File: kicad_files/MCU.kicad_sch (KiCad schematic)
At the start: 25 parts, among them SW1 SW_Push, SW2 SW_Push, U1 STM32F407VGTx, Y1 LFXTAL036869Reel 8MHz Crystal

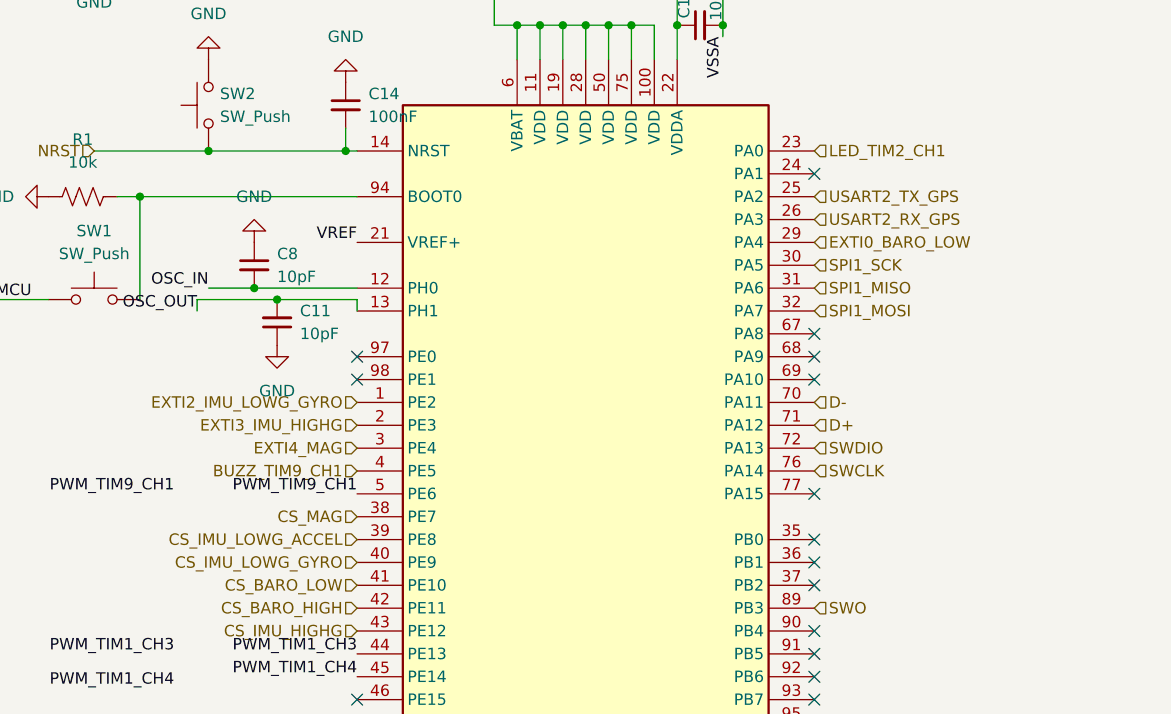
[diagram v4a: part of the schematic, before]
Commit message: switch sensor interrupts
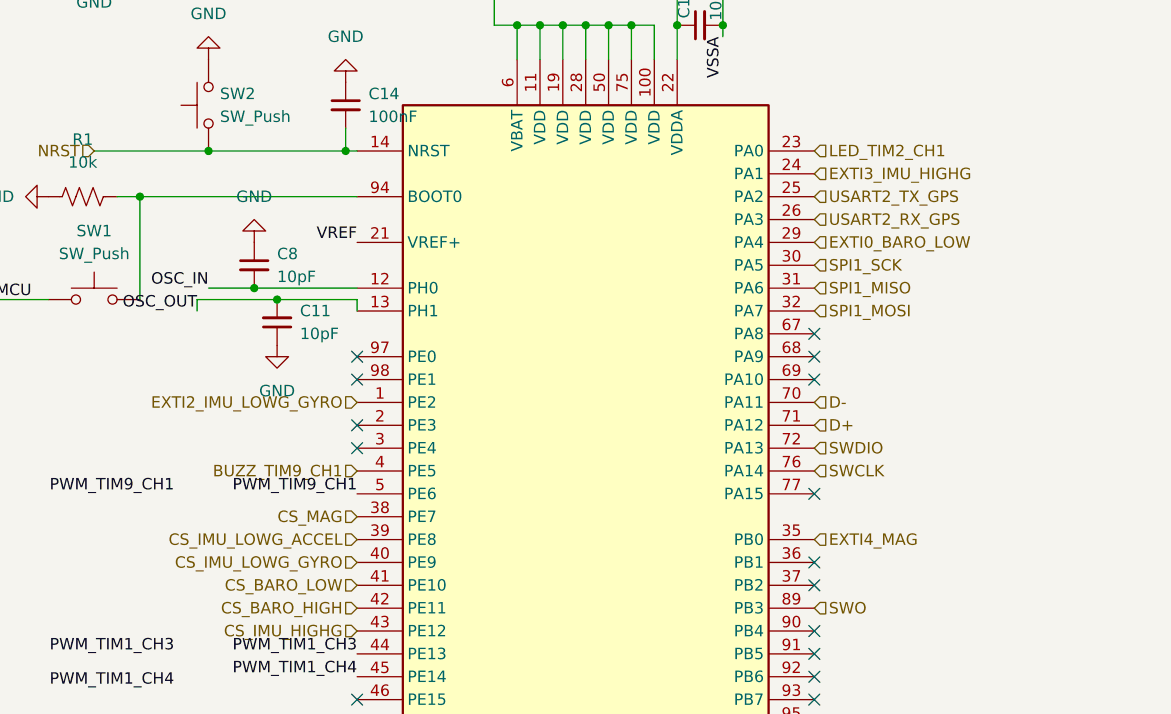
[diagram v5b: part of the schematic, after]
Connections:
- net EXTI3_IMU_HIGHG: now also U1.24 (PA1); no longer U1.2 (PE3)
- net EXTI4_MAG: now also U1.35 (PB0); no longer U1.3 (PE4)
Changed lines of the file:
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@@
-	)
-	(no_connect
-		(at 250.19 137.16)
 	)
 	(no_connect
@@
 	)
 	(no_connect
-		(at 250.19 96.52)
-	)
-	(no_connect
 		(at 250.19 119.38)
 	)
@@
 	)
 	(no_connect
+		(at 199.39 127)
+	)
+	(no_connect
 		(at 199.39 170.18)
 	)
@@
 	(no_connect
 		(at 199.39 185.42)
+	)
+	(no_connect
+		(at 199.39 124.46)
 	)
 	(no_connect
@@
 	(hierarchical_label "EXTI4_MAG"
 		(shape input)
-		(at 199.39 127 180)
-		(effects
-			(font
-				(size 1.27 1.27)
-			)
-			(justify right)
+		(at 250.19 137.16 0)
+		(effects
+			(font
+				(size 1.27 1.27)
+			)
+			(justify left)
 		)
 	)
@@
 	(hierarchical_label "EXTI3_IMU_HIGHG"
 		(shape input)
-		(at 199.39 124.46 180)
-		(effects
-			(font
-				(size 1.27 1.27)
-			)
-			(justify right)
-		)
-	)
+		(at 250.19 96.52 0)
+		(effects
+			(font
+				(size 1.27 1.27)
+			)
+			(justify left)
+		)
+	)

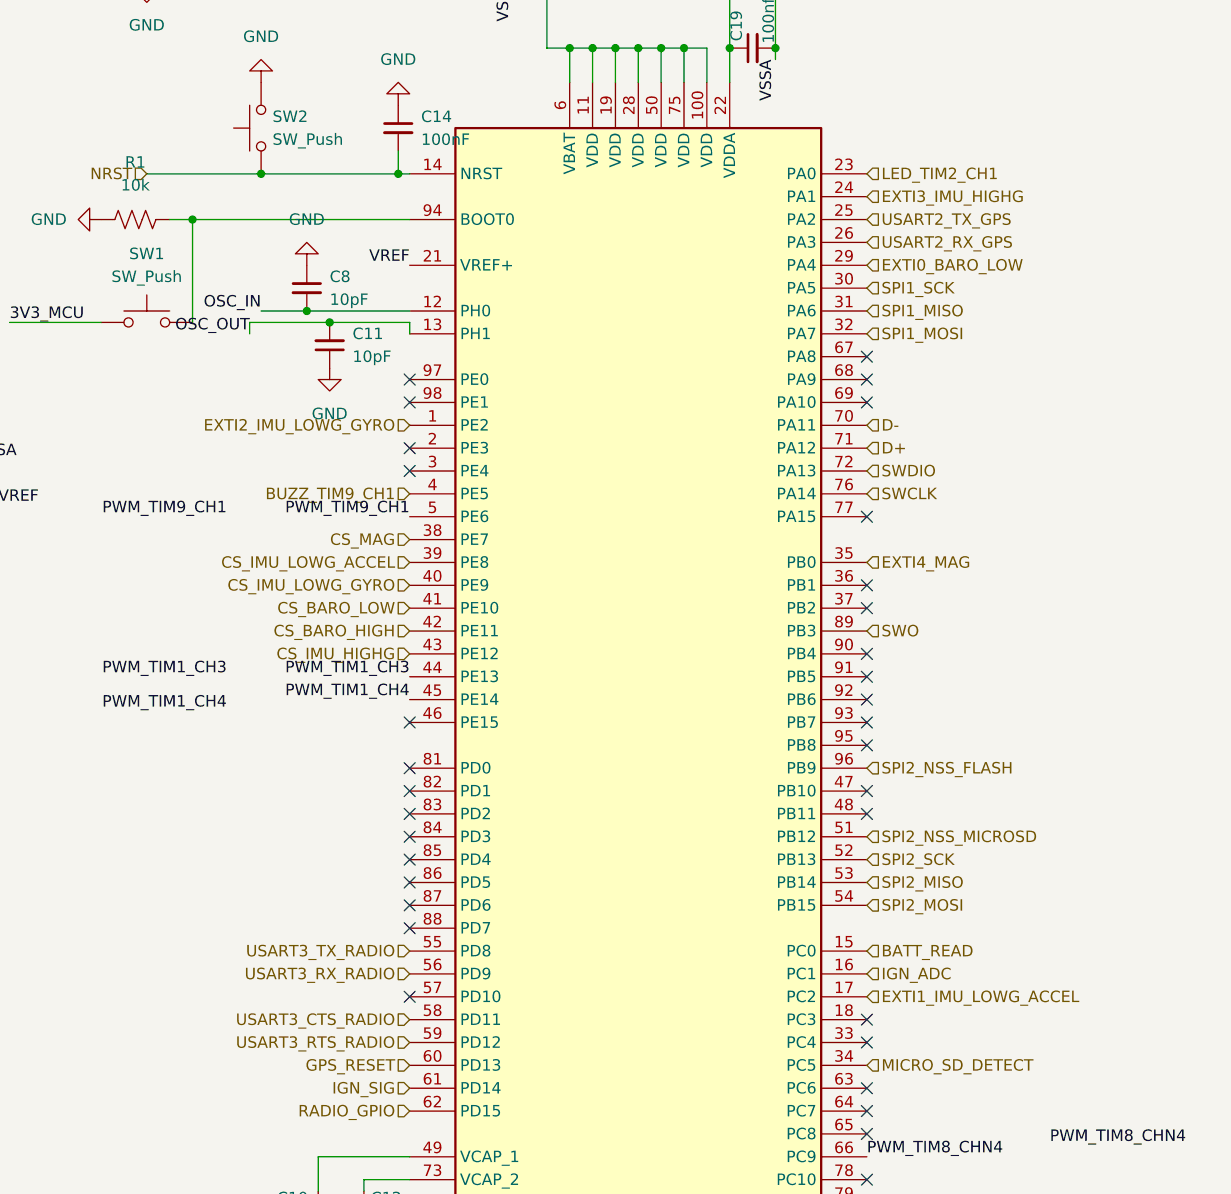
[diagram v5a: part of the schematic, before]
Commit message: changed led, tim
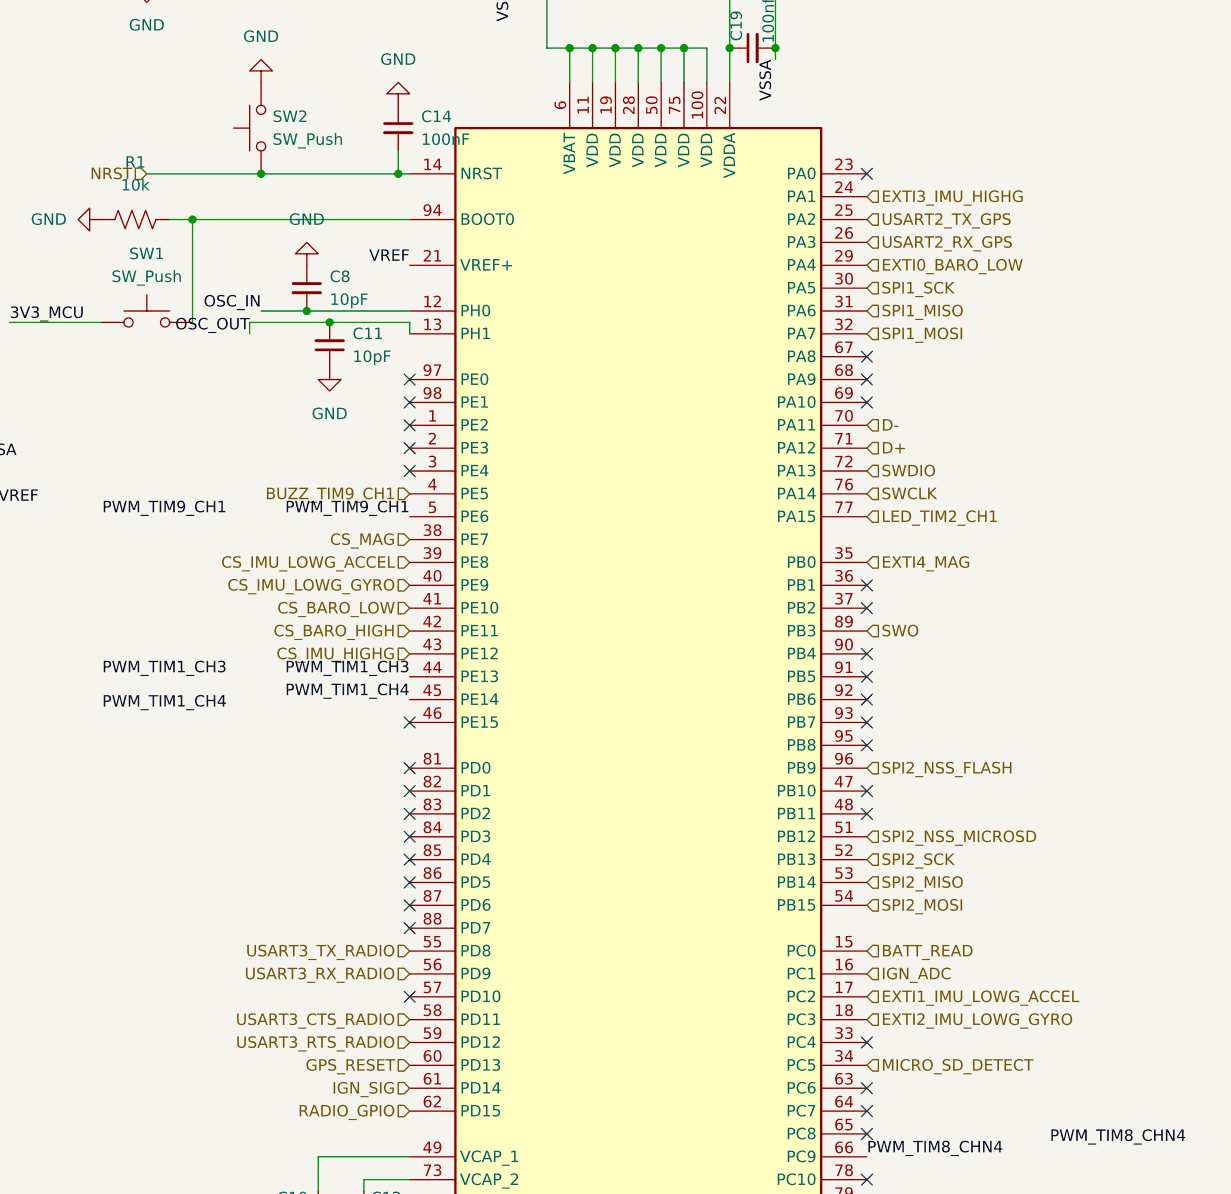
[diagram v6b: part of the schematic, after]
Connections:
- net EXTI2_IMU_LOWG_GYRO: now also U1.18 (PC3); no longer U1.1 (PE2)
- net LED_TIM2_CH1: now also U1.77 (PA15); no longer U1.23 (PA0)
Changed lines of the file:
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@@
-	)
-	(no_connect
-		(at 250.19 132.08)
 	)
 	(no_connect
@@
 	)
 	(no_connect
+		(at 199.39 121.92)
+	)
+	(no_connect
 		(at 250.19 152.4)
 	)
@@
 	)
 	(no_connect
+		(at 250.19 93.98)
+	)
+	(no_connect
 		(at 199.39 154.94)
 	)
@@
 	(no_connect
 		(at 199.39 177.8)
-	)
-	(no_connect
-		(at 250.19 187.96)
 	)
 	(no_connect
@@
 	(hierarchical_label "EXTI2_IMU_LOWG_GYRO"
 		(shape input)
-		(at 199.39 121.92 180)
+		(at 250.19 187.96 0)
+		(effects
+			(font
+				(size 1.27 1.27)
+			)
+			(justify left)
+		)
+	)
+	(hierarchical_label "CS_BARO_LOW"
+		(shape input)
+		(at 199.39 142.24 180)
 		(effects
 			(font
@@
 		)
 	)
-	(hierarchical_label "CS_BARO_LOW"
-		(shape input)
-		(at 199.39 142.24 180)
-		(effects
-			(font
-				(size 1.27 1.27)
-			)
-			(justify right)
-		)
-	)
 	(hierarchical_label "LED_TIM2_CH1"
 		(shape input)
-		(at 250.19 93.98 0)
-		(effects
-			(font
+		(at 250.19 132.08 0)
+		(effects
+			(font

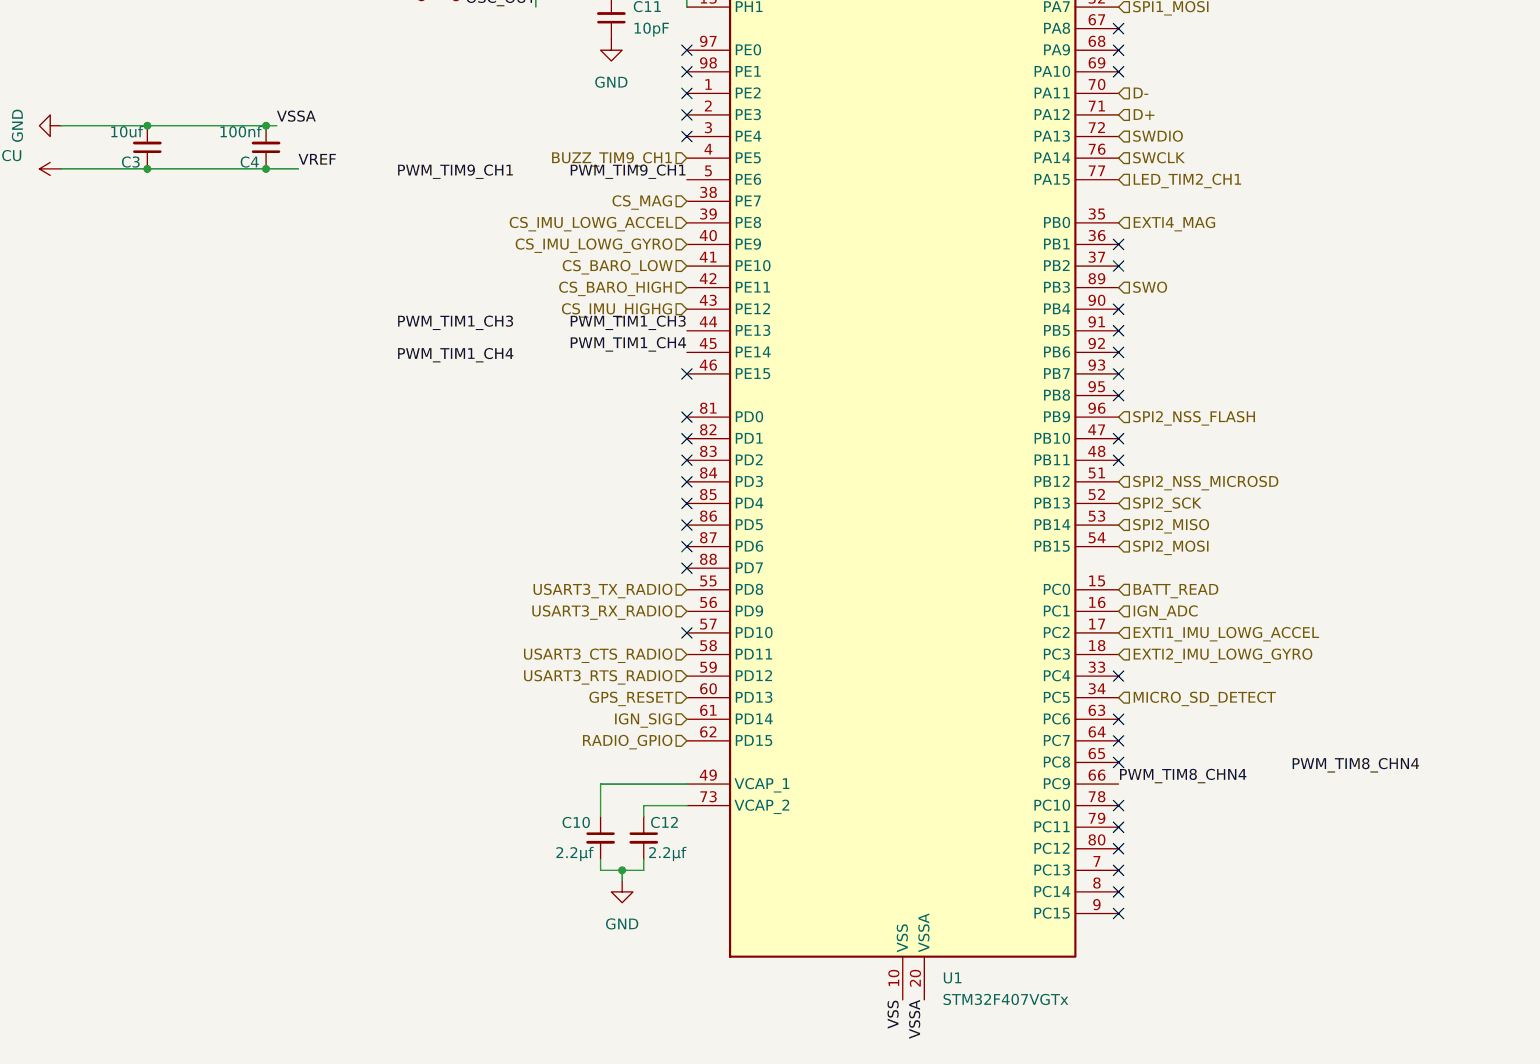
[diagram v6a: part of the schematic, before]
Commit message: complete rest of pin swaps
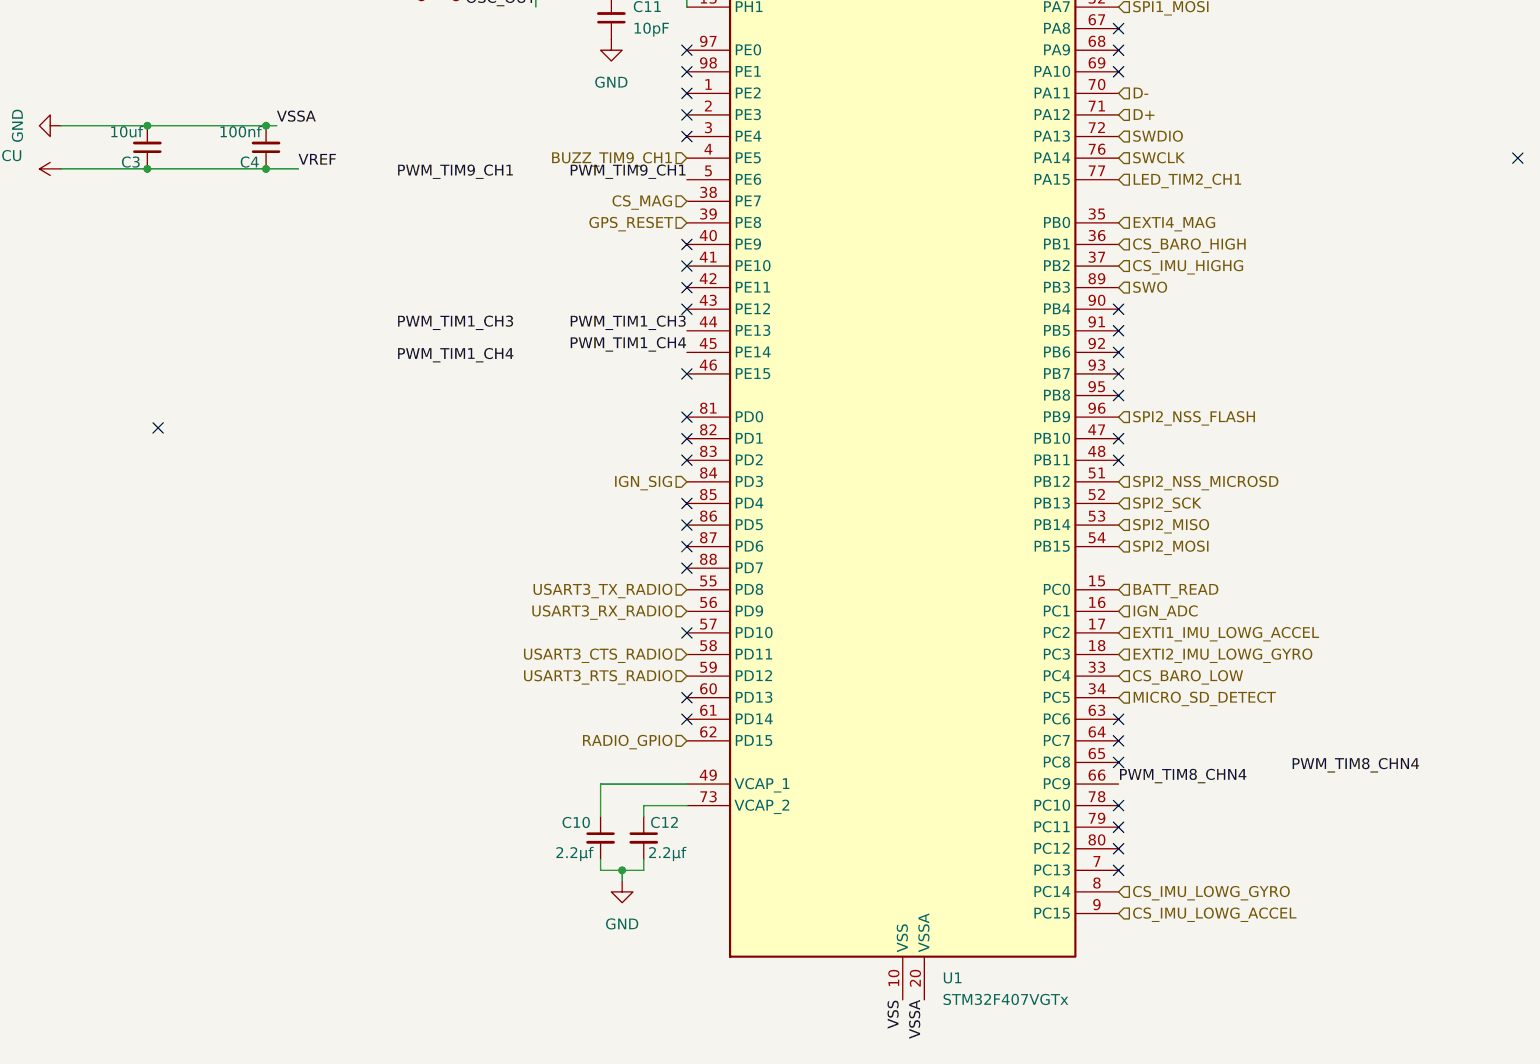
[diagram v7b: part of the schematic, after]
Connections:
- net CS_BARO_HIGH: now also U1.36 (PB1); no longer U1.42 (PE11)
- net CS_BARO_LOW: now also U1.33 (PC4); no longer U1.41 (PE10)
- net CS_IMU_HIGHG: now also U1.37 (PB2); no longer U1.43 (PE12)
- net CS_IMU_LOWG_ACCEL: now also U1.9 (PC15); no longer U1.39 (PE8)
- net CS_IMU_LOWG_GYRO: now also U1.8 (PC14); no longer U1.40 (PE9)
- net GPS_RESET: now also U1.39 (PE8); no longer U1.60 (PD13)
- net IGN_SIG: now also U1.84 (PD3); no longer U1.61 (PD14)
- no-connect marks 38 -> 40

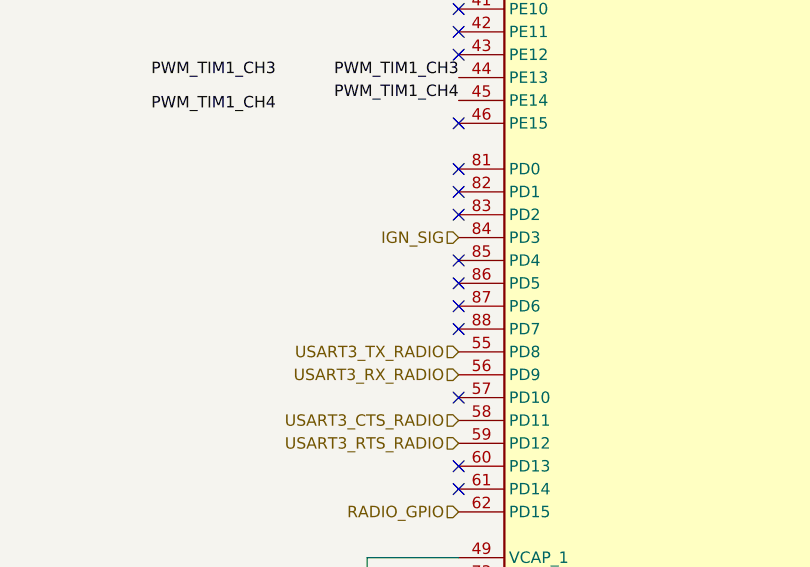
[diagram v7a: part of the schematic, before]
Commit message: Connect IGN2 signal, rearrange
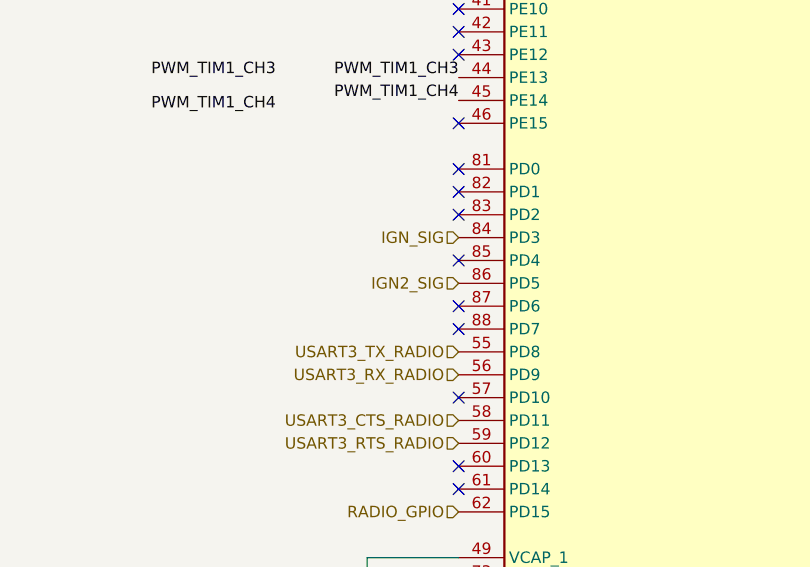
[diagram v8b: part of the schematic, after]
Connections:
- net IGN2_SIG: now reaches U1.86 (PD5)
- no-connect marks 40 -> 39
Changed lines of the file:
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@@
-	)
-	(no_connect
-		(at 199.39 172.72)
 	)
 	(no_connect
@@
 		)
 	)
+	(hierarchical_label "IGN2_SIG"
+		(shape input)
+		(at 199.39 172.72 180)
+		(effects
+			(font
+				(size 1.27 1.27)
+			)
+			(justify right)
+		)
+	)
